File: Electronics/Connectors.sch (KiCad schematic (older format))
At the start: 3 parts

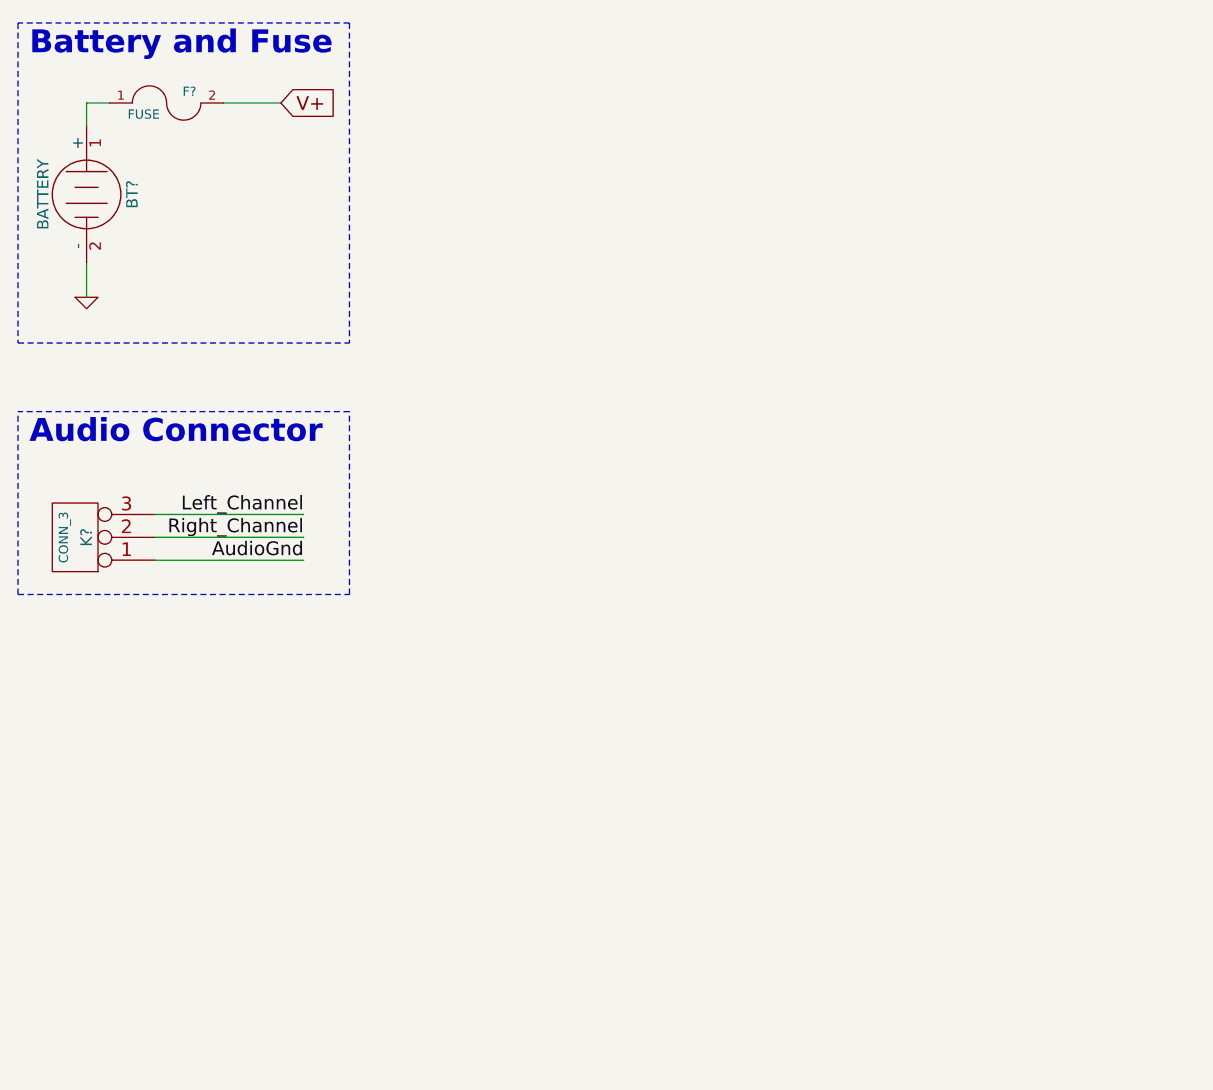
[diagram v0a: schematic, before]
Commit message: I think the first draft is done. Next step is to get a rough PCB setup.
Still need to find componets for all of the
caps, resistors, fuse, and connectors
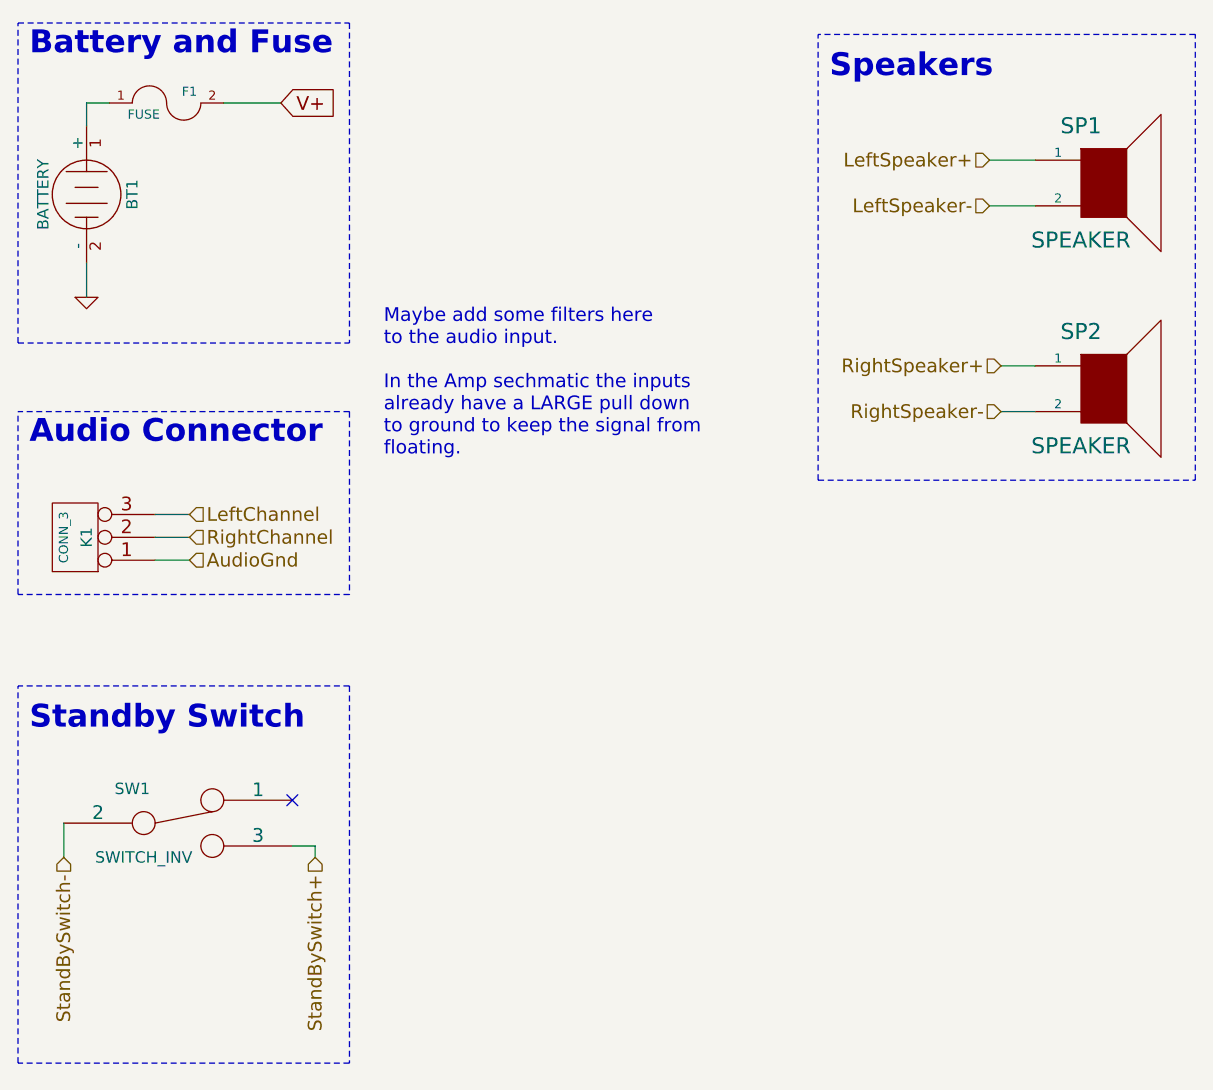
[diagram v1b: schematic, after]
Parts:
- added SP1, SP2: SPEAKER, symbol SPEAKER
- added SW1: SWITCH_INV, symbol SWITCH_INV
- gave numbers to parts that had none: 3
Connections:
- net Left_Channel renamed LeftChannel
- net Right_Channel renamed RightChannel
- new net LeftSpeaker+: SP1.1
- new net LeftSpeaker-: SP1.2
- new net RightSpeaker+: SP2.1
- new net RightSpeaker-: SP2.2
- new net StandBySwitch+: SW1.3
- new net StandBySwitch-: SW1.2
- no-connect marks 0 -> 1
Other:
- note added: "Maybe add some filters here\nto the audio input.\n\nIn the Amp sechmatic the inputs\nalready have a LARGE pull down\nto ground to keep the signal from\nfloating."
- note added: "Speakers"
- note added: "Standby Switch"
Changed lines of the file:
@@
-EESchema Schematic File Version 2  date 8/2/2012 3:30:21 PM
+EESchema Schematic File Version 2  date 8/2/2012 4:04:56 PM
 LIBS:power
 LIBS:device
@@
 $Descr A4 11700 8267
 encoding utf-8
-Sheet 2 4
+Sheet 3 5
 Title ""
 Date "2 aug 2012"
@@
 Comment4 ""
 $EndDescr
-Text Notes 700  2350 0    100  ~ 20
-Audio Connector
+Text Notes 2250 2400 0    60   ~ 0
+Maybe add some filters here\nto the audio input.\n\nIn the Amp sechmatic the inputs\nalready have a LARGE pull down\nto ground to keep the signal from\nfloating.
 Wire Notes Line
-	650  3000 650  2200
+	4150 2500 4150 550
 Wire Notes Line
-	650  3000 2100 3000
+	4150 2500 5800 2500
 Wire Notes Line
-	2100 3000 2100 2200
+	5800 2500 5800 550
 Wire Notes Line
-	2100 2200 650  2200
+	5800 550  4150 550
 Wire Wire Line
-	1250 2750 1900 2750
+	4950 2000 5100 2000
+Wire Wire Line
+	4900 1100 5100 1100
+Wire Wire Line
+	1950 4150 1950 4100
+Wire Wire Line
+	1950 4100 1850 4100
+Wire Wire Line
+	1250 2850 1400 2850
+Wire Wire Line
+	1250 2650 1400 2650
+Wire Notes Line
+	650  1900 2100 1900
+Wire Wire Line
+	950  1550 950  1700
+Wire Wire Line
+	950  950  950  850
+Wire Wire Line
+	950  850  1050 850
+Wire Wire Line
+	1550 850  1800 850
+Wire Notes Line
+	650  1900 650  500
+Wire Notes Line
+	650  500  2100 500
 Wire Notes Line
 	2100 500  2100 1900
 Wire Notes Line
-	2100 500  650  500
+	2100 2200 650  2200
 Wire Notes Line
-	650  500  650  1900
+	2100 2200 2100 3000
+Wire Notes Line
+	2100 3000 650  3000
+Wire Notes Line
+	650  3000 650  2200
 Wire Wire Line
-	1550 850  1800 850
+	1250 2750 1400 2750
 Wire Wire Line
-	1050 850  950  850
+	850  4150 850  4000
+Wire Notes Line
+	2100 3400 650  3400
+Wire Notes Line
+	2100 3400 2100 5050
+Wire Notes Line
+	2100 5050 650  5050
+Wire Notes Line
+	650  5050 650  3400
 Wire Wire Line
-	950  850  950  950
+	4900 1300 5100 1300
 Wire Wire Line
-	950  1550 950  1700
-Wire Notes Line
-	650  1900 2100 1900
-Wire Wire Line
-	1250 2650 1900 2650
-Wire Wire Line
-	1250 2850 1900 2850
-Text Label 1900 2850 2    60   ~ 0
+	4950 2200 5100 2200
+Text Notes 4200 750  0    100  ~ 20
+Speakers
+Text HLabel 4950 2200 0    60   Input ~ 0
+RightSpeaker-
+Text HLabel 4950 2000 0    60   Input ~ 0
+RightSpeaker+
+Text HLabel 4900 1300 0    60   Input ~ 0
+LeftSpeaker-
+Text HLabel 4900 1100 0    60   Input ~ 0
+LeftSpeaker+
+$Comp
+L SPEAKER SP2
+U 1 1 501AE822
+P 5400 2100
+F 0 "SP2" H 5300 2350 70  0000 C CNN
+F 1 "SPEAKER" H 5300 1850 70  0000 C CNN
+	1    5400 2100
+	1    0    0    -1
+$EndComp
+$Comp
+L SPEAKER SP1
+U 1 1 501AE81D
+P 5400 1200
+F 0 "SP1" H 5300 1450 70  0000 C CNN
+F 1 "SPEAKER" H 5300 950 70  0000 C CNN
+	1    5400 1200
+	1    0    0    -1
+$EndComp
+Text Notes 700  3600 0    100  ~ 20
+Standby Switch
+NoConn ~ 1850 3900
+Text HLabel 1950 4150 3    60   Input ~ 0
+StandBySwitch+
+Text HLabel 850  4150 3    60   Input ~ 0
+StandBySwitch-
+$Comp
+L SWITCH_INV SW1
+U 1 1 501AE6F6
+P 1350 4000
+F 0 "SW1" H 1150 4150 50  0000 C CNN
+F 1 "SWITCH_INV" H 1200 3850 50  0000 C CNN
+	1    1350 4000
+	1    0    0    -1
+$EndComp
+Text HLabel 1400 2850 2    60   Input ~ 0
 AudioGnd
-Text Label 1900 2750 2    60   ~ 0
-Right_Channel
-Text Label 1900 2650 2    60   ~ 0
-Left_Channel
+Text HLabel 1400 2750 2    60   Input ~ 0
+RightChannel
+Text HLabel 1400 2650 2    60   Input ~ 0
+LeftChannel
+Text Notes 700  2350 0    100  ~ 20
+Audio Connector
 $Comp
-L CONN_3 K?
+L CONN_3 K1
 U 1 1 501AE2BE
 P 900 2750
-F 0 "K?" V 850 2750 50  0000 C CNN
+F 0 "K1" V 850 2750 50  0000 C CNN
 F 1 "CONN_3" V 950 2750 40  0000 C CNN
 	1    900  2750
@@
 V+
 $Comp
-L GND #PWR?
+L GND #PWR1
 U 1 1 501ADFC4
 P 950 1700
-F 0 "#PWR?" H 950 1700 30  0001 C CNN
+F 0 "#PWR1" H 950 1700 30  0001 C CNN
 F 1 "GND" H 950 1630 30  0001 C CNN
 	1    950  1700
@@
 $EndComp
 $Comp
-L FUSE F?
+L FUSE F1
 U 1 1 501ADFA8
 P 1300 850
-F 0 "F?" H 1400 900 40  0000 C CNN
+F 0 "F1" H 1400 900 40  0000 C CNN
 F 1 "FUSE" H 1200 800 40  0000 C CNN
 	1    1300 850
@@
 $EndComp
 $Comp
-L BATTERY BT?
+L BATTERY BT1
 U 1 1 501ADF0F
 P 950 1250
-F 0 "BT?" H 950 1450 50  0000 C CNN
+F 0 "BT1" H 950 1450 50  0000 C CNN
 F 1 "BATTERY" H 950 1060 50  0000 C CNN
 	1    950  1250
